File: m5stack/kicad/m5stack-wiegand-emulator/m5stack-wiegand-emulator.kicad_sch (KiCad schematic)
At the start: 23 parts, among them J1 2x15 socket header, J2 2x15 pin header, J3 1x5 female, U1 RP2040, U2 6N135S, U3 6N135S, U4 6N135S

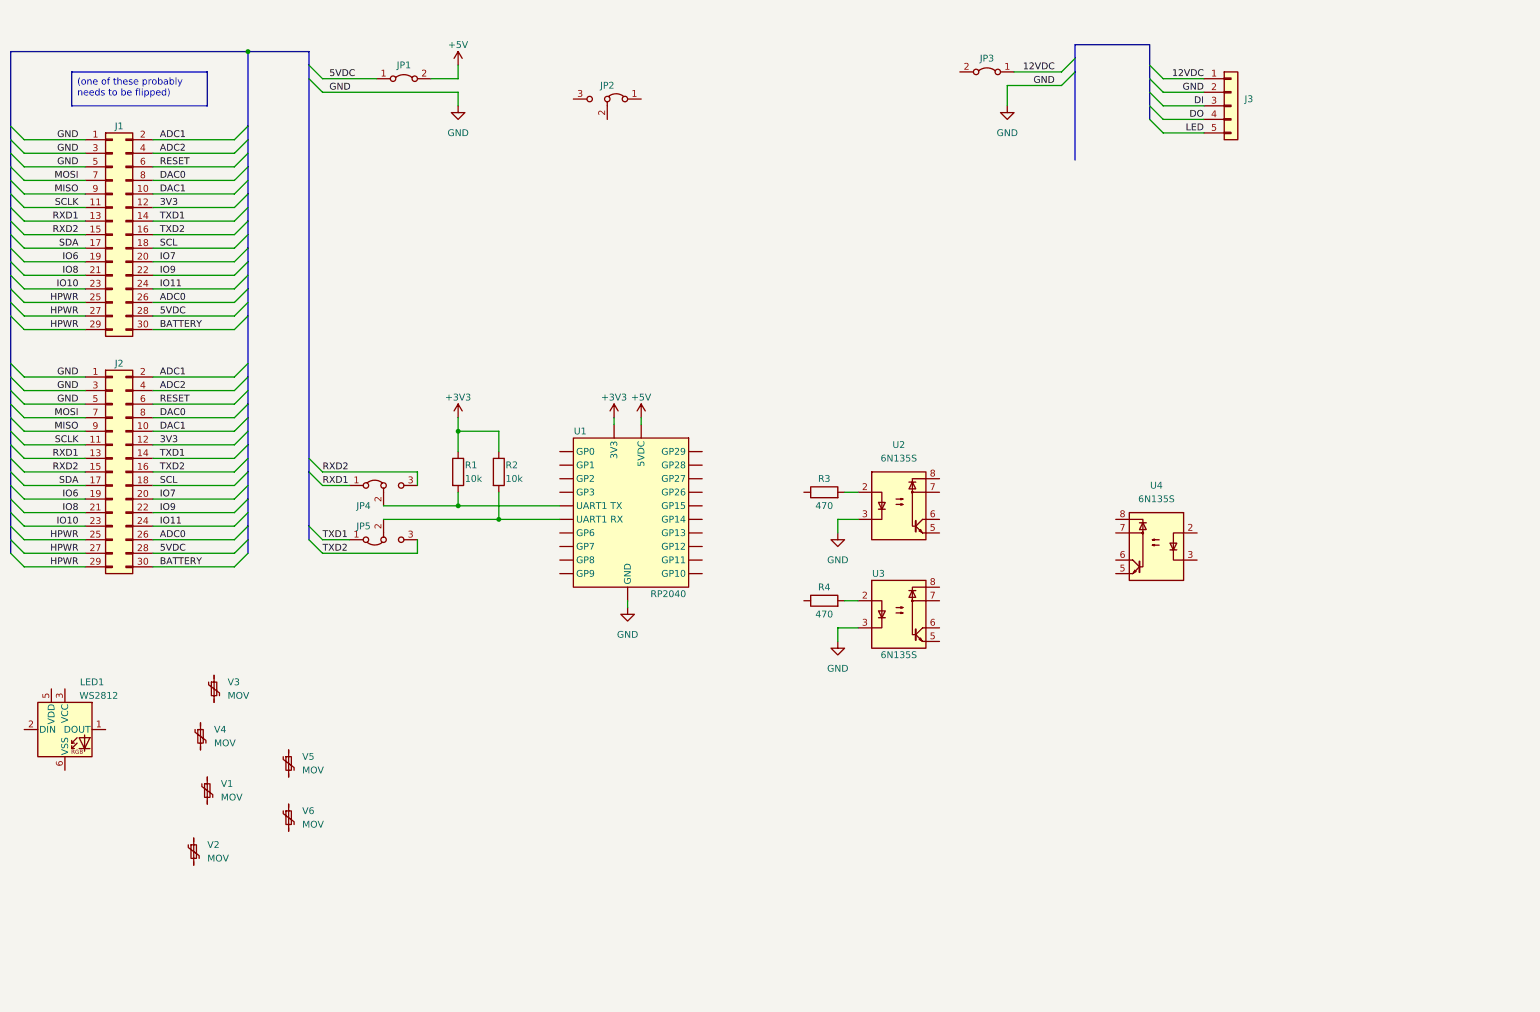
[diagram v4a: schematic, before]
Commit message: M5: reworking WS2812 to use SN74HCT245
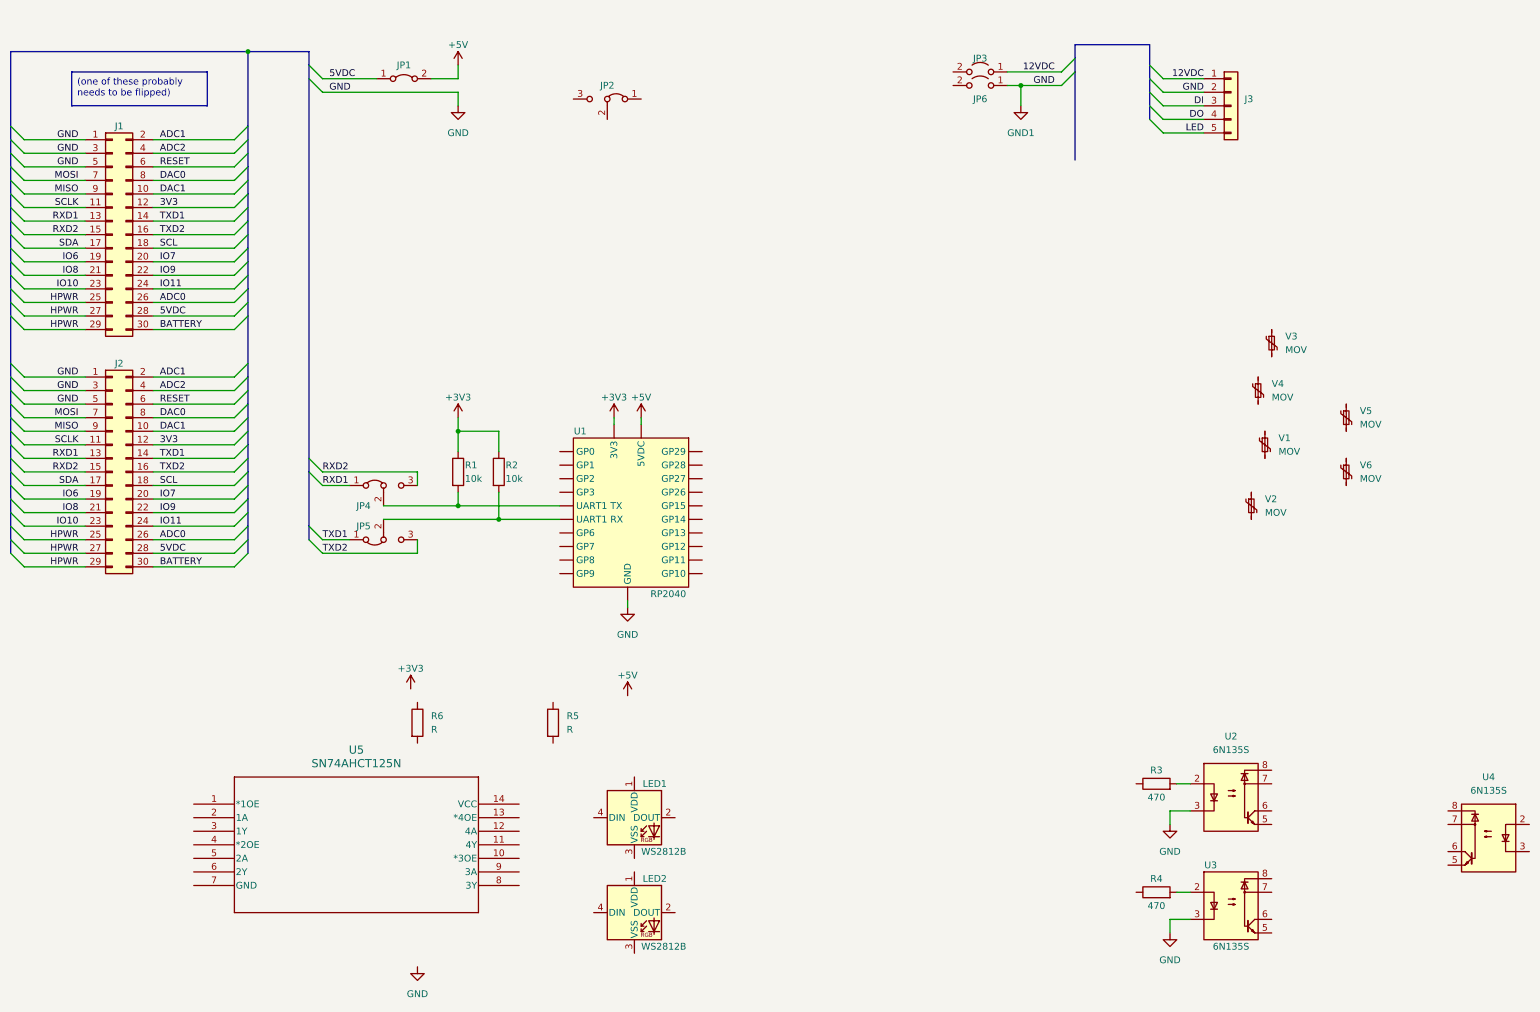
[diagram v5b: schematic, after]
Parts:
- added JP6: Jumper_2_Bridged, symbol Jumper:Jumper_2_Open
- added LED2: WS2812B, LED_SMD:LED_WS2812B_PLCC4_5.0x5.0mm_P3.2mm, symbol LED:WS2812B
- added R5, R6: R, symbol Device:R
- added U5: SN74AHCT125N, N14, symbol uhppoted:SN74AHCT125N
- JP3: symbol Jumper:Jumper_2_Bridged -> Jumper:Jumper_2_Open
- LED1: value WS2812 -> WS2812B; footprint LED_SMD:LED_WS2812_PLCC6_5.0x5.0mm_P1.6mm -> LED_SMD:LED_WS2812B_PLCC4_5.0x5.0mm_P3.2mm; symbol LED:WS2812 -> LED:WS2812B
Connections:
- net GND: now also JP6.1 (A)
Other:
- moved on the sheet: JP3, R3, R4, U2, U3, U4, V1, V2, V3, V4, V5, V6

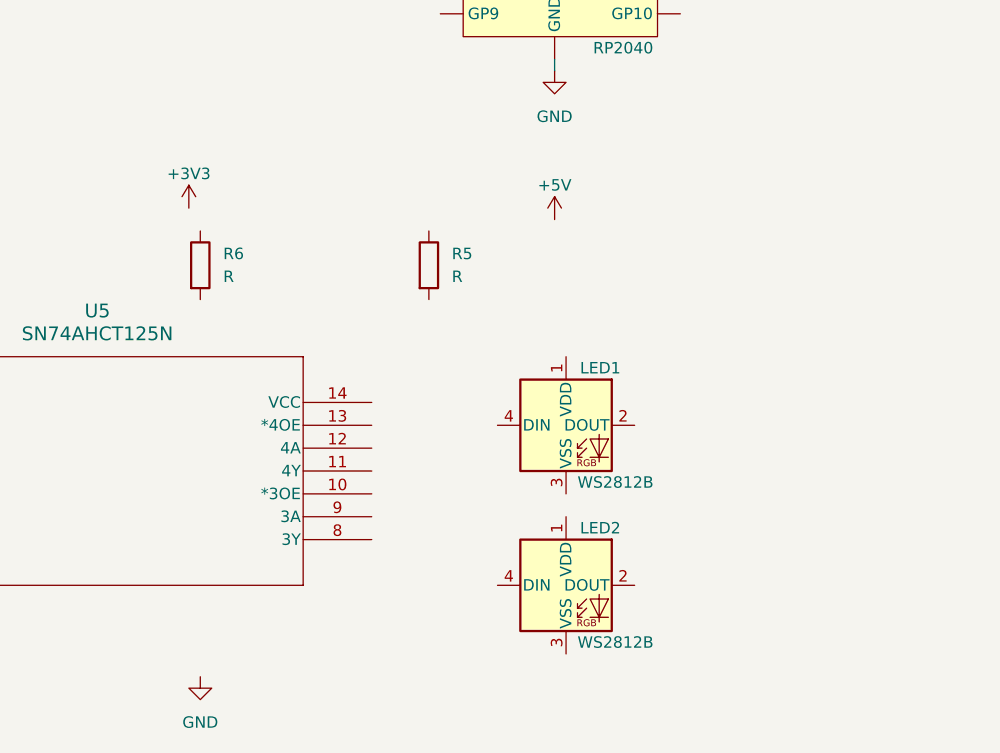
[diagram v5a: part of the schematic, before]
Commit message: M5: reworking LEDs to use SN74HCTx124 level translation
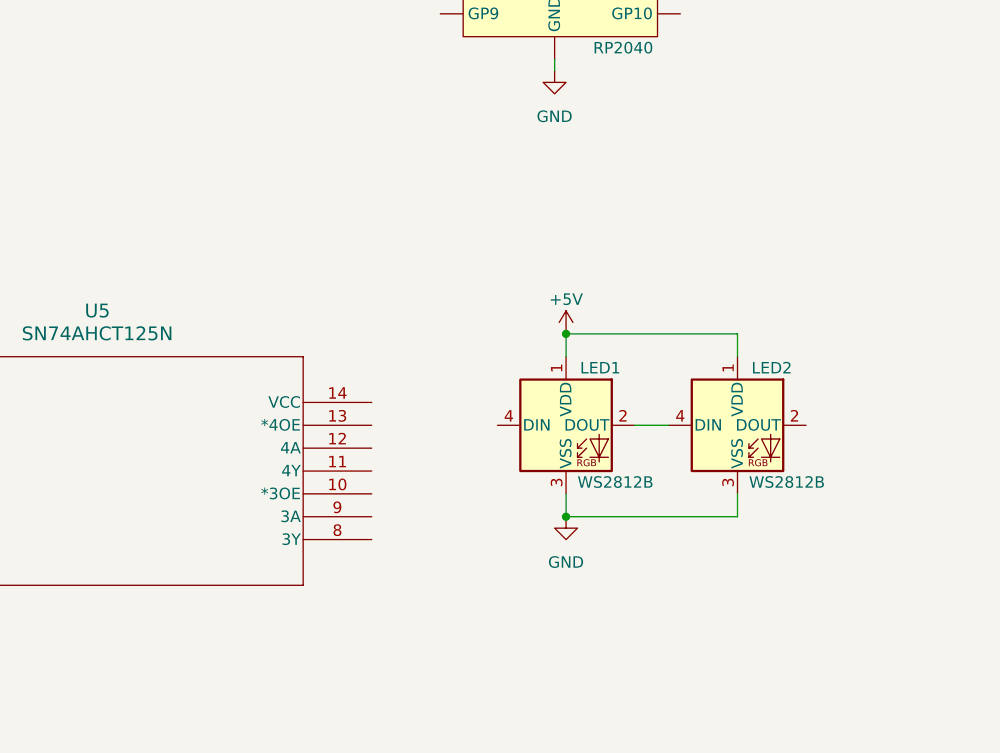
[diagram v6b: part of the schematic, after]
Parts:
- removed R5, R6: R, symbol Device:R
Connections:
- net +5V: now also LED1.1 (VDD), LED2.1 (VDD)
- net GND: now also LED1.3 (VSS), LED2.3 (VSS)
- net at LED1.2 (DOUT): now also LED2.4 (DIN)
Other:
- moved on the sheet: LED2
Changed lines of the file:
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@@
   (junction (at 120.65 113.03) (diameter 0) (color 0 0 0 0)
   )
+  (junction (at 146.05 179.07) (diameter 0) (color 0 0 0 0)
+  )
   (junction (at 113.03 110.49) (diameter 0) (color 0 0 0 0)
   )
+  (junction (at 146.05 158.75) (diameter 0) (color 0 0 0 0)
+  )
   (bus_entry (at 29.21 88.9) (size 2.54 2.54)
     (stroke (width 0) (type default))
@@
     (stroke (width 0) (type default))
   )
+  (wire (pts (xy 146.05 158.75) (xy 146.05 161.29))
+    (stroke (width 0) (type default))
+  )
   (wire (pts (xy 31.75 88.9) (xy 43.18 88.9))
     (stroke (width 0) (type default))
@@
     (stroke (width 0) (type default))
   )
+  (wire (pts (xy 165.1 158.75) (xy 146.05 158.75))
+    (stroke (width 0) (type default))
+  )
   (wire (pts (xy 31.75 116.84) (xy 43.18 116.84))
     (stroke (width 0) (type default))
@@
     (stroke (width 0) (type default))
   )
+  (wire (pts (xy 165.1 179.07) (xy 146.05 179.07))
+    (stroke (width 0) (type default))
+  )
   (bus (pts (xy 73.66 74.93) (xy 73.66 83.82))
     (stroke (width 0) (type default))
@@
     (stroke (width 0) (type default))
   )
+  (wire (pts (xy 165.1 176.53) (xy 165.1 179.07))
+    (stroke (width 0) (type default))
+  )
   (bus (pts (xy 29.21 44.45) (xy 29.21 46.99))
     (stroke (width 0) (type default))
@@
     (stroke (width 0) (type default))
   )
+  (wire (pts (xy 153.67 168.91) (xy 157.48 168.91))
+    (stroke (width 0) (type default))
+  )
   (wire (pts (xy 31.75 41.91) (xy 43.18 41.91))
     (stroke (width 0) (type default))
@@
     (stroke (width 0) (type default))
   )
+  (wire (pts (xy 146.05 176.53) (xy 146.05 179.07))
+    (stroke (width 0) (type default))
+  )
   (wire (pts (xy 31.75 109.22) (xy 43.18 109.22))
     (stroke (width 0) (type default))
@@
   )
   (bus (pts (xy 73.66 64.77) (xy 73.66 67.31))
+    (stroke (width 0) (type default))
+  )
+  (wire (pts (xy 165.1 161.29) (xy 165.1 158.75))
     (stroke (width 0) (type default))
   )
@@
   (label "ADC1" (at 57.15 86.36 0) (fields_autoplaced)
     (effects (font (size 1.27 1.27)) (justify left bottom))
-  )
-  (symbol (lib_id "Device:R") (at 130.81 151.13 0) (unit 1)
-    (in_bom yes) (on_board yes) (dnp no) (fields_autoplaced)
-    (property "Reference" "R5" (at 133.35 149.86 0)
-      (effects (font (size 1.27 1.27)) (justify left))
-    )
-    (property "Value" "R" (at 133.35 152.4 0)
-      (effects (font (size 1.27 1.27)) (justify left))
-    )
-    (property "Footprint" "" (at 129.032 151.13 90)
-      (effects (font (size 1.27 1.27)) hide)
-    )
-    (property "Datasheet" "~" (at 130.81 151.13 0)
-      (effects (font (size 1.27 1.27)) hide)
-    )
-    (pin "1")
-    (pin "2")
-    (instances
-      (project "m5stack-wiegand-emulator"
-        (path "/591217c3-ab1f-4851-a185-c0f7ee9f3d97"
-          (reference "R5") (unit 1)
-        )
-      )
-    )
   )
   (symbol (lib_id "uhppoted:MOV") (at 261.62 110.49 0) (unit 1)
@@
         (path "/591217c3-ab1f-4851-a185-c0f7ee9f3d97"
           (reference "LED1") (unit 1)
-        )
-      )
-    )
-  )
-  (symbol (lib_id "Device:R") (at 105.41 151.13 0) (unit 1)
-    (in_bom yes) (on_board yes) (dnp no) (fields_autoplaced)
-    (property "Reference" "R6" (at 107.95 149.86 0)
-      (effects (font (size 1.27 1.27)) (justify left))
-    )
-    (property "Value" "R" (at 107.95 152.4 0)
-      (effects (font (size 1.27 1.27)) (justify left))
-    )
-    (property "Footprint" "" (at 103.632 151.13 90)
-      (effects (font (size 1.27 1.27)) hide)
-    )
-    (property "Datasheet" "~" (at 105.41 151.13 0)
-      (effects (font (size 1.27 1.27)) hide)
-    )
-    (pin "1")
-    (pin "2")
-    (instances
-      (project "m5stack-wiegand-emulator"
-        (path "/591217c3-ab1f-4851-a185-c0f7ee9f3d97"
-          (reference "R6") (unit 1)
         )
       )
@@
     )
   )
-  (symbol (lib_id "power:GND") (at 105.41 196.85 0) (mirror y) (unit 1)
+  (symbol (lib_id "power:GND") (at 146.05 179.07 0) (mirror y) (unit 1)
     (in_bom yes) (on_board yes) (dnp no) (fields_autoplaced)
-    (property "Reference" "#PWR011" (at 105.41 203.2 0)
-      (effects (font (size 1.27 1.27)) hide)
-    )
-    (property "Value" "GND" (at 105.41 201.93 0)
-      (effects (font (size 1.27 1.27)))
-    )
-    (property "Footprint" "" (at 105.41 196.85 0)
-      (effects (font (size 1.27 1.27)) hide)
-    )
-    (property "Datasheet" "" (at 105.41 196.85 0)
+    (property "Reference" "#PWR011" (at 146.05 185.42 0)
+      (effects (font (size 1.27 1.27)) hide)
+    )
+    (property "Value" "GND" (at 146.05 184.15 0)
+      (effects (font (size 1.27 1.27)))
+    )
+    (property "Footprint" "" (at 146.05 179.07 0)
+      (effects (font (size 1.27 1.27)) hide)
+    )
+    (property "Datasheet" "" (at 146.05 179.07 0)
       (effects (font (size 1.27 1.27)) hide)
     )
@@
     )
   )
-  (symbol (lib_id "LED:WS2812B") (at 146.05 186.69 0) (unit 1)
-    (in_bom yes) (on_board yes) (dnp no)
-    (property "Reference" "LED2" (at 149.86 180.34 0)
-      (effects (font (size 1.27 1.27)))
-    )
-    (property "Value" "WS2812B" (at 147.32 193.04 0)
-      (effects (font (size 1.27 1.27)) (justify left))
-    )
-    (property "Footprint" "LED_SMD:LED_WS2812B_PLCC4_5.0x5.0mm_P3.2mm" (at 147.32 194.31 0)
+  (symbol (lib_id "LED:WS2812B") (at 165.1 168.91 0) (unit 1)
+    (in_bom yes) (on_board yes) (dnp no)
+    (property "Reference" "LED2" (at 168.91 162.56 0)
+      (effects (font (size 1.27 1.27)))
+    )
+    (property "Value" "WS2812B" (at 166.37 175.26 0)
+      (effects (font (size 1.27 1.27)) (justify left))
+    )
+    (property "Footprint" "LED_SMD:LED_WS2812B_PLCC4_5.0x5.0mm_P3.2mm" (at 166.37 176.53 0)
       (effects (font (size 1.27 1.27)) (justify left top) hide)
     )
-    (property "Datasheet" "https://cdn-shop.adafruit.com/datasheets/WS2812B.pdf" (at 148.59 196.215 0)
+    (property "Datasheet" "https://cdn-shop.adafruit.com/datasheets/WS2812B.pdf" (at 167.64 178.435 0)
       (effects (font (size 1.27 1.27)) (justify left top) hide)
     )
@@
     )
   )
-  (symbol (lib_id "power:+5V") (at 144.78 146.05 0) (mirror y) (unit 1)
-    (in_bom yes) (on_board yes) (dnp no)
-    (property "Reference" "#PWR09" (at 144.78 149.86 0)
-      (effects (font (size 1.27 1.27)) hide)
-    )
-    (property "Value" "+5V" (at 144.78 142.24 0)
-      (effects (font (size 1.27 1.27)))
-    )
-    (property "Footprint" "" (at 144.78 146.05 0)
-      (effects (font (size 1.27 1.27)) hide)
-    )
-    (property "Datasheet" "" (at 144.78 146.05 0)
+  (symbol (lib_id "power:+5V") (at 146.05 158.75 0) (mirror y) (unit 1)
+    (in_bom yes) (on_board yes) (dnp no)
+    (property "Reference" "#PWR09" (at 146.05 162.56 0)
+      (effects (font (size 1.27 1.27)) hide)
+    )
+    (property "Value" "+5V" (at 146.05 154.94 0)
+      (effects (font (size 1.27 1.27)))
+    )
+    (property "Footprint" "" (at 146.05 158.75 0)
+      (effects (font (size 1.27 1.27)) hide)
+    )
+    (property "Datasheet" "" (at 146.05 158.75 0)
       (effects (font (size 1.27 1.27)) hide)
     )
@@
         )
       )
-    )
-  )
-  (symbol (lib_id "power:+3V3") (at 104.14 144.78 0) (unit 1)
-    (in_bom yes) (on_board yes) (dnp no)
-    (property "Reference" "#PWR012" (at 104.14 148.59 0)
-      (effects (font (size 1.27 1.27)) hide)
-    )
-    (property "Value" "+3V3" (at 104.14 140.97 0)
-      (effects (font (size 1.27 1.27)))
-    )
-    (property "Footprint" "" (at 104.14 144.78 0)
-      (effects (font (size 1.27 1.27)) hide)
-    )
-    (property "Datasheet" "" (at 104.14 144.78 0)
-      (effects (font (size 1.27 1.27)) hide)
-    )
-    (pin "1")
-    (instances
-      (project "m5stack-wiegand-emulator"
-        (path "/591217c3-ab1f-4851-a185-c0f7ee9f3d97"
-          (reference "#PWR012") (unit 1)
-        )
-      )
